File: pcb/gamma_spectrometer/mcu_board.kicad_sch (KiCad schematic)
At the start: 39 parts, among them U301 TL431DBZ, U302 STM32G474MET6, U303 W25Q64JVSSIQ, Y301 ABM8G-16.000MHZ-4Y-T3

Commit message: Complete BOM: MPN and footprints for all components
Session 5 (2026-05-23) - full BOM assignment finished.

Components assigned (KiCad Symbol Fields + Footprints):
- 81 capacitors / 17 unique MPN (Yageo, Murata, Vishay, Holy Stone)
- 79 resistors / 28 unique MPN (Yageo RC/RT/RL/AC series)
- 3 inductors (Bourns SRN3015 + SRU5028)
- 2 LEDs (Foryard + Wurth 0805)
- 1 PTC fuse (MF-MSMF050-2)
- 1 ferrite bead (Murata BLM18EG121SN1D, 0603 - fixed from docs 0402)
- All active ICs (STM32G474, MAX1847, AD8000, FT231XQ, etc.)

Key design decisions:
- Standard bypass: 100nF X7R 0603 (easier hand soldering vs 0402)
- LED package 0805 (instead of 0402)
- C115 consolidated with C206 on single MPN (GRM32ER71A476KE15L)
- HV chain (1812 1kV X7R, 18x): Holy Stone C1812X104K102T
- AD8000 Cfb: GRM1555C1H1R0WA01D 1pF +/-0.05pF NP0
- R415: 50R -> 49.9R E96 (50R unavailable in catalog)
- L101/L102: SRN3015 (footprint Neosid SMS-ME3015, geometry verified)
- L103: SRU5028 (footprint L_Bourns_SRU5016, XY identical)

Documentation contradictions fixed:
- C115 MPN: GRM32ER61A476KE20L -> GRM32ER71A476KE15L
- FT231XS (SSOP-16) -> FT231XQ (QFN-20) - actual chip choice
- Tantalum MPN: TAJA106K016RNJ -> TR3B106K010C0750 (Vishay Low ESR)
- Inductor refs in usb_power_board_schematic.md updated

Remaining for PCB order:
- D202/D203 footprint: change SOD-123W -> SOD-123 (Diotec standard)
- J_PMT401: custom B14-38 footprint (during PCB layout)

Files:
- bom_fp_work.md - authoritative BOM with status, MPN, footprints, URLs
- pcb/gamma_spectrometer.net - fresh netlist with all MPN fields
- docs/session_context.md - session 5 final state

Co-Authored-By: Claude Sonnet 4.6 <noreply@anthropic.com>
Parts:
- C301, C302: footprint (none) -> Capacitor_SMD:C_0402_1005Metric_Pad0.74x0.62mm_HandSolder; PN (none) -> CC0402FRNPO9BN180; Ссылка на покупку  (none) -> https://www.electronshik.ru/item/YAG/CC0402FRNPO9BN180
- C303, C304, C305, C306, C307, C308, C309, C311, C312, C313, C314, C317, C319, C320, C321: value 100nF -> 0.1uF; footprint (none) -> Capacitor_SMD:C_0603_1608Metric_Pad1.08x0.95mm_HandSolder; PN (none) -> CC0603JRX7R9BB104; Ссылка на покупку  (none) -> https://www.electronshik.ru/item/YAG/CC0603JRX7R9BB104
- C310: footprint (none) -> Capacitor_SMD:C_0805_2012Metric_Pad1.18x1.45mm_HandSolder; PN (none) -> GRM21BR61C475KA88L; Ссылка на покупку  (none) -> https://www.electronshik.ru/item/MUR/GRM21BR61C475KA88L
- C315, C318: footprint (none) -> Capacitor_SMD:C_0603_1608Metric_Pad1.08x0.95mm_HandSolder; PN (none) -> CC0603JRNPO9BN101; Ссылка на покупку  (none) -> https://www.electronshik.ru/item/YAG/CC0603JRNPO9BN101
- C316: footprint (none) -> Capacitor_SMD:C_0603_1608Metric_Pad1.08x0.95mm_HandSolder; PN (none) -> CC0603FRNPO9BN511; Ссылка на покупку  (none) -> https://www.electronshik.ru/item/YAG/CC0603FRNPO9BN511
- FB301: footprint (none) -> Inductor_SMD:L_0603_1608Metric_Pad1.05x0.95mm_HandSolder; PN (none) -> BLM18EG121SN1D; Ссылка на покупку  (none) -> https://www.electronshik.ru/item/MUR/BLM18EG121SN1D
- R301: footprint (none) -> Resistor_SMD:R_0603_1608Metric_Pad0.98x0.95mm_HandSolder; PN (none) -> RC0603FR-07470RL; Ссылка на покупку  (none) -> https://www.electronshik.ru/item/YAG/RC0603FR-07470RL
- R302, R303, R304, R305, R307, R309: footprint (none) -> Resistor_SMD:R_0603_1608Metric_Pad0.98x0.95mm_HandSolder; PN (none) -> RC0603FR-0710KL; Ссылка на покупку  (none) -> https://www.electronshik.ru/item/YAG/RC0603FR-0710KL
- R306, R308: footprint (none) -> Resistor_SMD:R_0603_1608Metric_Pad0.98x0.95mm_HandSolder; PN (none) -> RC0603FR-071KL; Ссылка на покупку  (none) -> https://www.electronshik.ru/item/YAG/RC0603FR-071KL
- R310: footprint (none) -> Resistor_SMD:R_0603_1608Metric_Pad0.98x0.95mm_HandSolder; PN (none) -> RC0603FR-0722KL; Ссылка на покупку  (none) -> https://www.electronshik.ru/item/YAG/RC0603FR-0722KL
- R311: footprint (none) -> Resistor_SMD:R_0603_1608Metric_Pad0.98x0.95mm_HandSolder; PN (none) -> RC0603FR-075K9L; Ссылка на покупку  (none) -> https://www.electronshik.ru/item/YAG/RC0603FR-075K9L
- R312: footprint (none) -> Resistor_SMD:R_0603_1608Metric_Pad0.98x0.95mm_HandSolder; PN (none) -> RC0603FR-078K2L; Ссылка на покупку  (none) -> https://www.electronshik.ru/item/YAG/RC0603FR-078K2L
- R313: footprint (none) -> Resistor_SMD:R_0603_1608Metric_Pad0.98x0.95mm_HandSolder; PN (none) -> RC0603FR-072KL; Ссылка на покупку  (none) -> https://www.electronshik.ru/item/YAG/RC0603FR-072KL
- U301: value TL431DBZ -> TL431; PN (none) -> TL431; Ссылка на покупку  (none) -> https://www.electronshik.ru/item/YOUTAI/TL431
- U302: PN (none) -> STM32G474MET6
- U303: PN (none) -> W25Q64JVSSIQ
- Y301: PN (none) -> ABM8G-16.000MHZ-4Y-T3

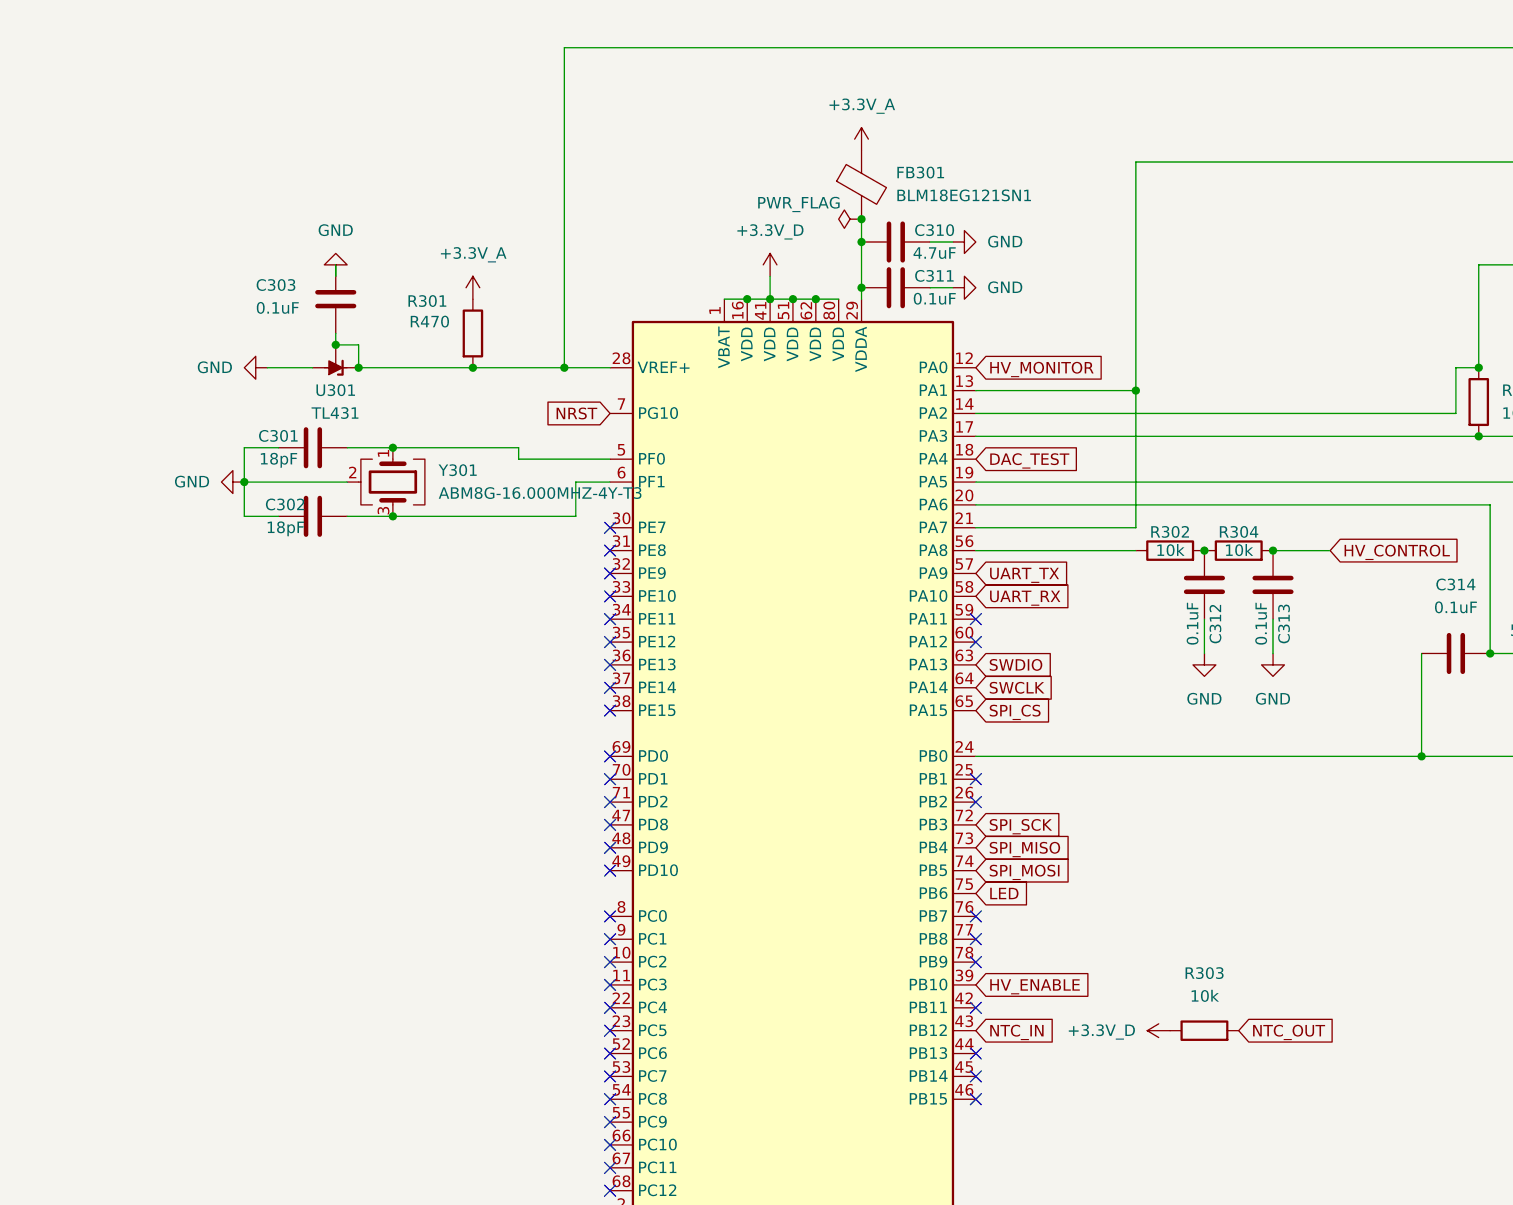
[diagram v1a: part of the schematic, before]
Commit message: Fix 2 critical schematic bugs found by full netlist audit
Full audit of all 191 nets (sessions 7-8, 2026-06-10/11) against design docs.

CRITICAL FIXES (schematic + netlist):
1. UART was straight-through, not crossed: FTDI TXD tied to PA9 (both
   outputs), RXD to PA10 (both inputs) - no communication possible.
   ERC missed it (MCU pins are bidirectional). Now: PA9(TX)->UART_RX
   ->FTDI RXD, FTDI TXD->UART_TX->PA10(RX).
2. PMT divider active buffers were dead: chain junctions were merged
   with dynodes DY6/7/8, so base resistors bridged base to own emitter
   (Vbe=0 forever, MMBTA42 never conducts). Now: dynode = emitter only;
   chain junction -> base resistor -> base; storage caps between dynode
   lines; collectors one stage up. Control nets listed in divider_board.md.
3. R301: 470 -> 330 ohm (ratiometric Pt1000 added 0.225mA load on TL431
   cathode; remaining current was at the 1mA minimum).

Also:
- Pt1000 connected ratiometrically (R303 pullup from TL431 cathode) -
  reference drift cancels out of temperature measurement
- R414 chain bottom goes to GND directly (not via anode/Rin) - docs
  updated to match schematic (cleaner: divider current bypasses signal node)
- cheatsheet_mistakes.md: new rules #7 (UART cross), #8 (dynode=emitter
  only), #9 (recalculate TL431 cathode current when loading VREF node)
- New docs: ad4084_dpp_design.md (v2 DPP upgrade spec, deferred),
  reference_spectra.md (baseline spectra analysis from user's current
  Sypher spectrometer: Cs-137, Lu-176, Am-241, Ra-226, Th-232)
- Datasheets added: AD4084, LTC2387-16/18
- Session context updated (sessions 7-8)

Known leftover: R301 purchase URL in KiCad still points to 470RL part.

Co-Authored-By: Claude Fable 5 <noreply@anthropic.com>
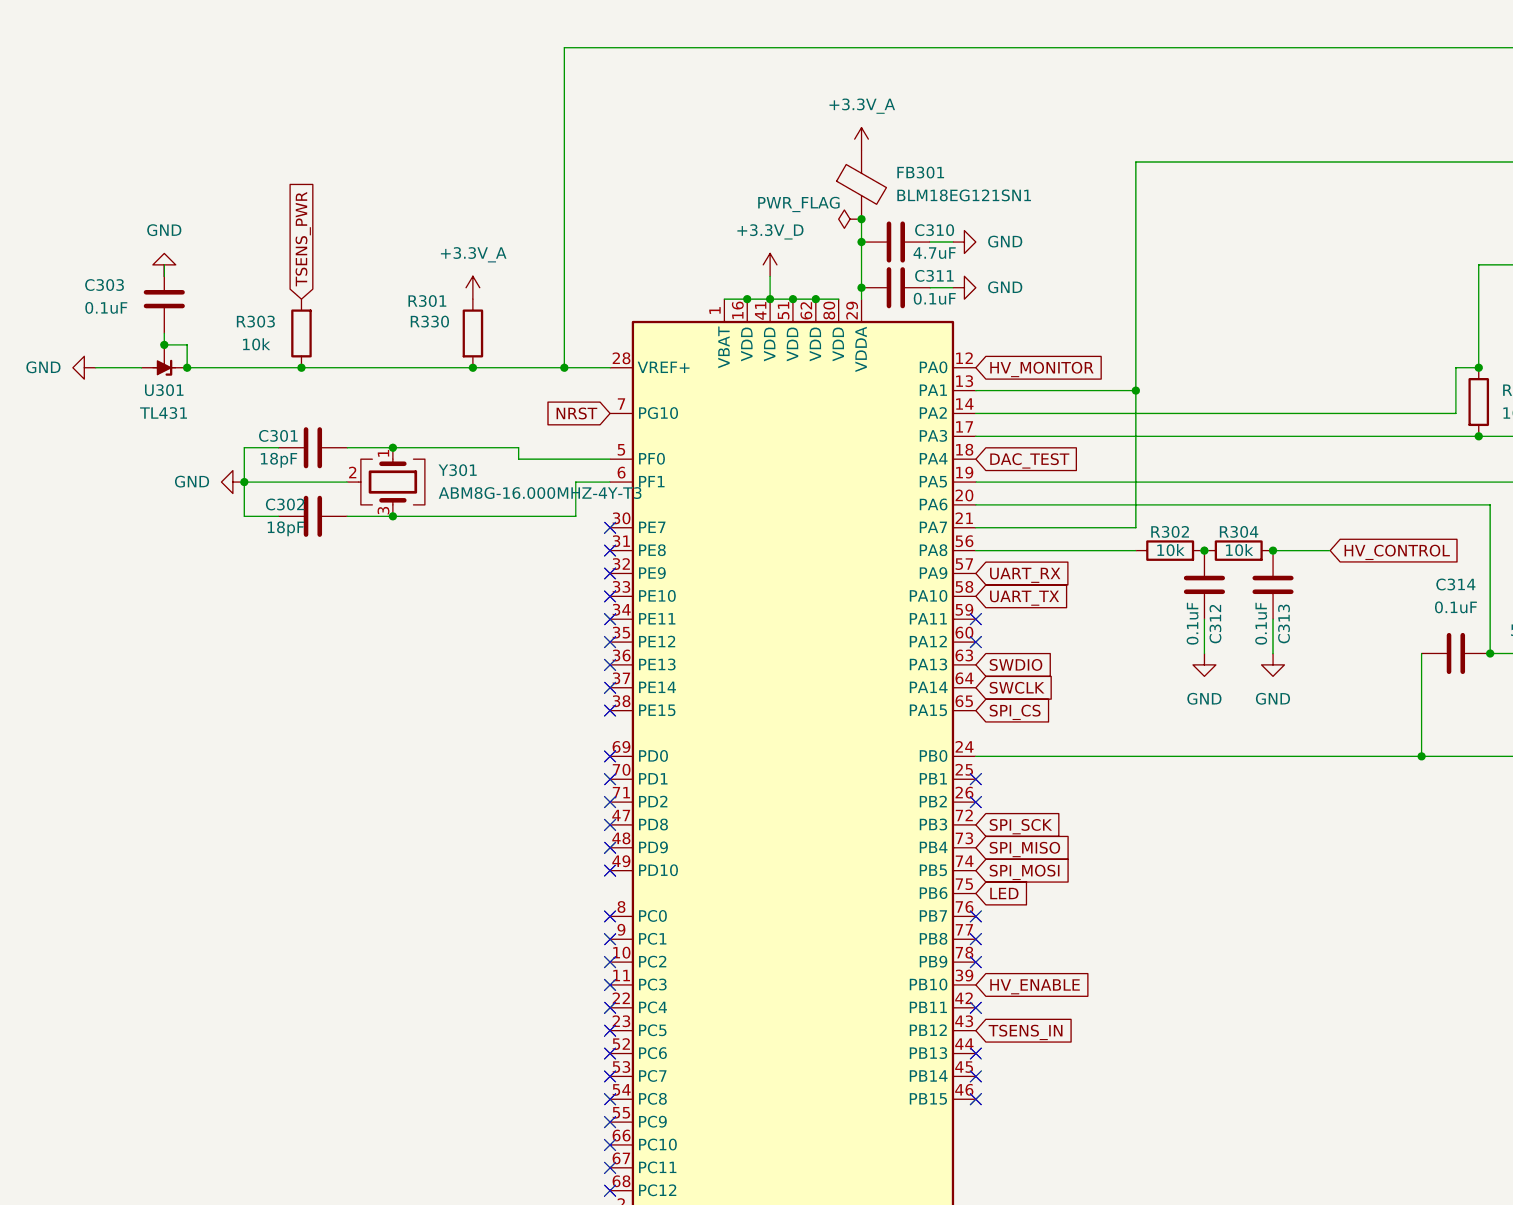
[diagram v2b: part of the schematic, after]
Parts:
- R301: value R470 -> R330; PN RC0603FR-07470RL -> RC0603FR-07330RL
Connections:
- net +3.3V_D: no longer R303.1
- net UART_RX: now also U302.57 (PA9); no longer U302.58 (PA10)
- net UART_TX: now also U302.58 (PA10); no longer U302.57 (PA9)
- net at C303.2, R301.2, R310.1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: now also R303.1
- net NTC_IN renamed TSENS_IN
- net NTC_OUT renamed TSENS_PWR
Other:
- moved on the sheet: C303, R303, U301

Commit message: session_context: quick-start block for context compaction recovery
Also: R301 purchase URL fix in mcu_board schematic (user edit, was pending).

Co-Authored-By: Claude Fable 5 <noreply@anthropic.com>
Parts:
- R301: Ссылка на покупку  https://www.electronshik.ru/item/YAG/RC0603FR-07470RL -> https://www.electronshik.ru/item/YAG/RC0603FR-07330RL
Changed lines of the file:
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@@
 			)
 		)
-		(property "Ссылка на покупку " "https://www.electronshik.ru/item/YAG/RC0603FR-07470RL"
+		(property "Ссылка на покупку " "https://www.electronshik.ru/item/YAG/RC0603FR-07330RL"
 			(at 232.41 127 0)
 			(effects
